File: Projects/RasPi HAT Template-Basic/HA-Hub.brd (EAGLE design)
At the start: 65 x 56 mm, 1 part, among them X1 RASPI_BOARD_B+_H

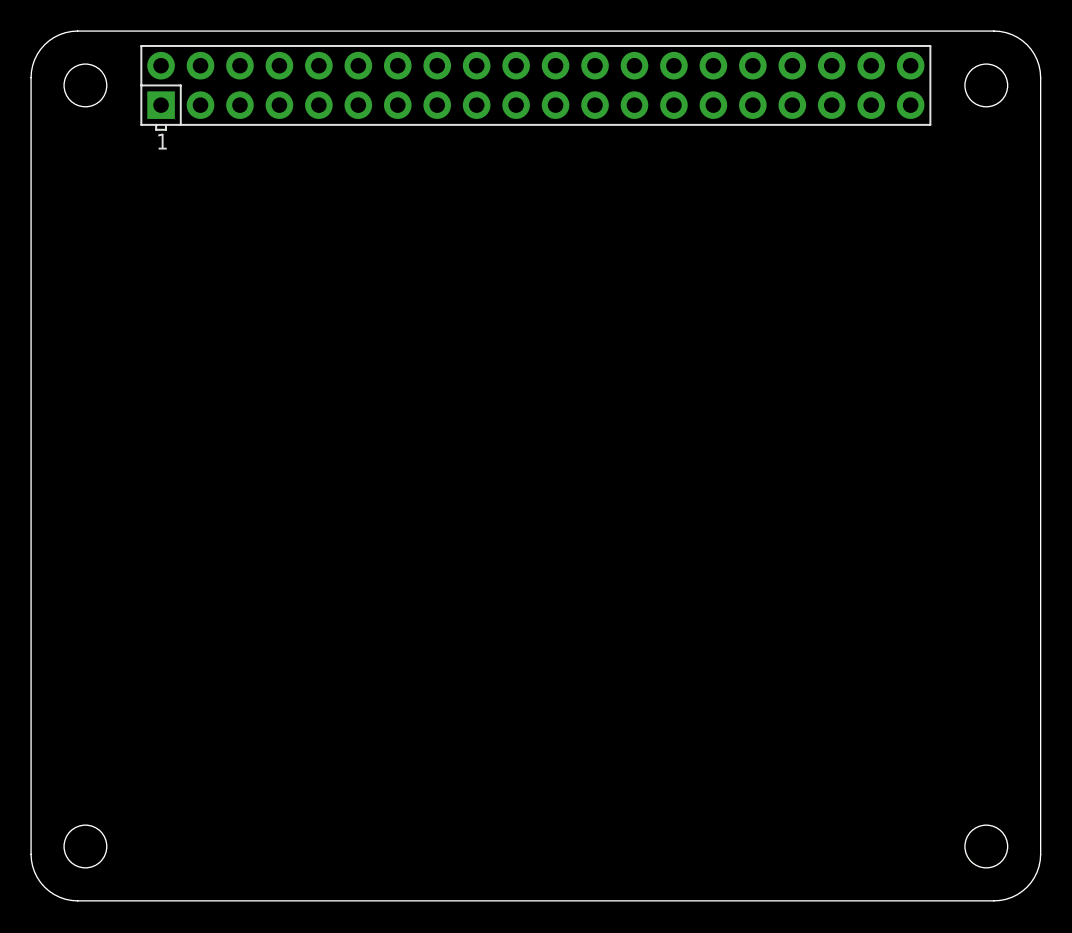
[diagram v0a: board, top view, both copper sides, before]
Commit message: Changed v1.3 board 'via' drill size to 13mil. Plus some house keeping,
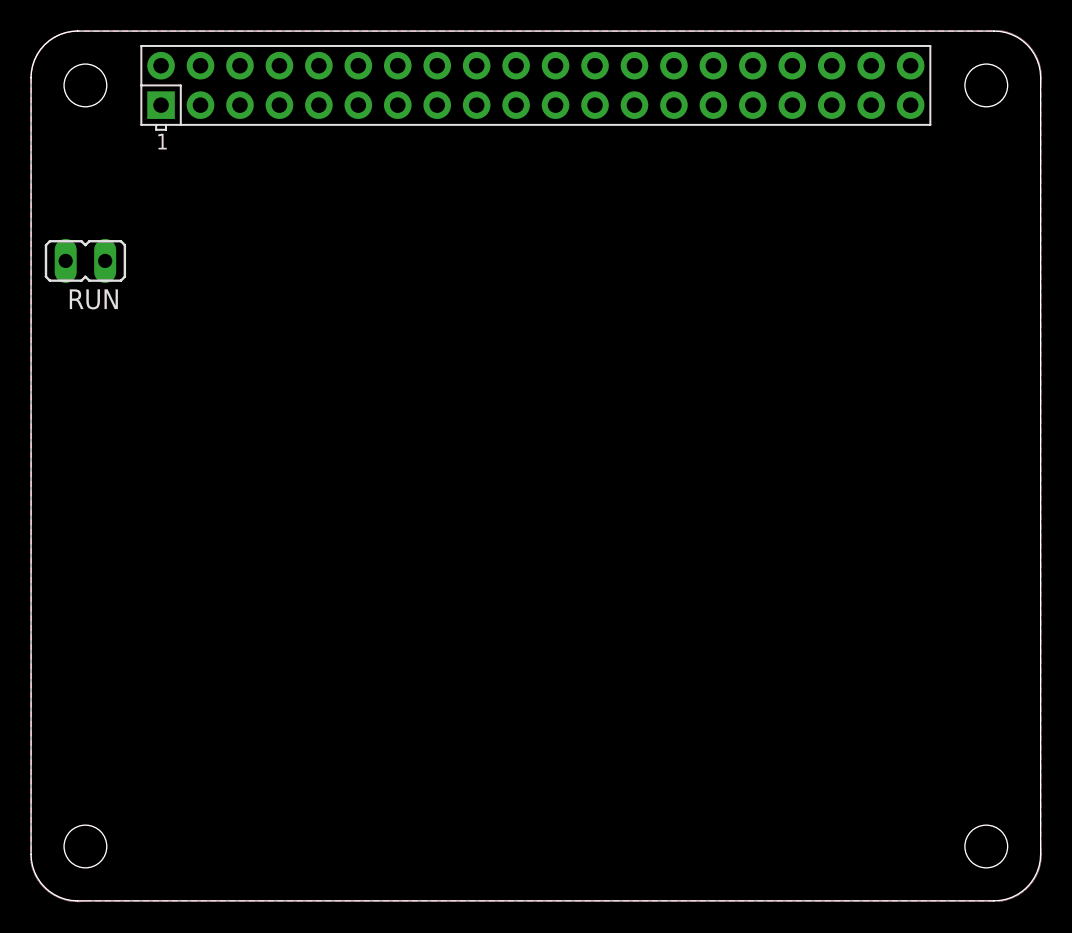
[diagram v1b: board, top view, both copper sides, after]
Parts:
- added RUN: RST, jumper:JP1
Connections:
- net 3V3 renamed +3V3
- net 5V0 renamed +5V
- new net RST: RUN.2
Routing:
- added copper zone on layer 1, net N$1
- added copper zone on layer 16, net N$1
